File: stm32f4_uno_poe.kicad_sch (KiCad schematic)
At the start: 13 parts, among them J101 STM32 GPIO, J102 Digital/PWM, J103 STM32 GPIO, J104 STM32 GPIO, J105 STM32 GPIO, J106 Power, J107 Conn_01x04, J108 Ethernet, J109 STM32 GPIO, J110 Digital/PWM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

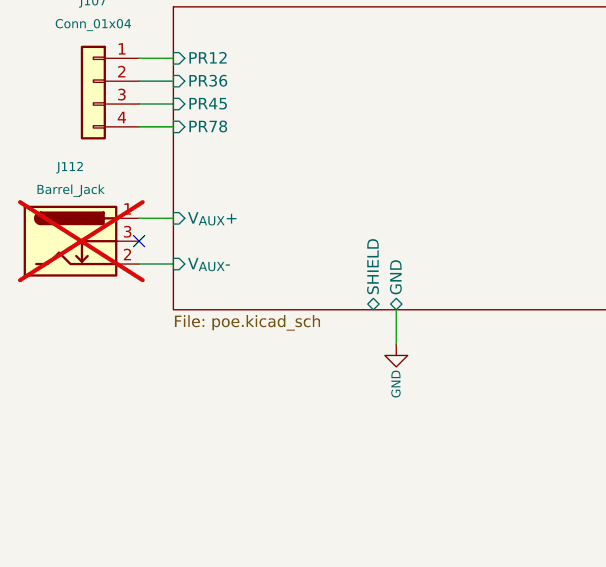
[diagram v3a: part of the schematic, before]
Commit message: Set DNP
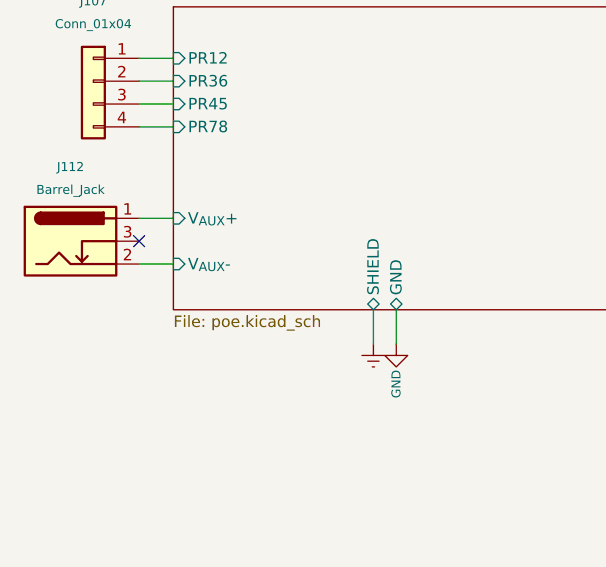
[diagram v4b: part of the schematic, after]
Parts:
- J104, J106, J107, J108, J111, J113: now left out of the parts list
- J112: now fitted; now left out of the parts list
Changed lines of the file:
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@@
     (stroke (width 0) (type solid))
+  )
+  (wire (pts (xy 85.725 85.09) (xy 85.725 88.9))
+    (stroke (width 0) (type default))
   )
   (wire (pts (xy 267.335 29.845) (xy 280.035 29.845))
@@
   )
   (symbol (lib_id "Connector_Generic:Conn_01x08") (at 189.865 45.085 0) (unit 1)
-    (in_bom yes) (on_board yes) (dnp no)
+    (in_bom no) (on_board yes) (dnp no)
     (property "Reference" "J106" (at 189.865 34.925 0)
       (effects (font (size 1 1)))
@@
     (property "Datasheet" "" (at 189.865 45.085 0)
       (effects (font (size 1 1)))
+    )
+    (property "Description" "" (at 189.865 45.085 0)
+      (effects (font (size 1.27 1.27)) hide)
+    )
+    (property "Manufacturer" "" (at 189.865 45.085 0)
+      (effects (font (size 1.27 1.27)) hide)
+    )
+    (property "Partnumber" "" (at 189.865 45.085 0)
+      (effects (font (size 1.27 1.27)) hide)
+    )
+    (property "JLCPCB Part #" "" (at 189.865 45.085 0)
+      (effects (font (size 1.27 1.27)) hide)
+    )
+    (property "isBasicPart" "" (at 189.865 45.085 0)
+      (effects (font (size 1.27 1.27)) hide)
+    )
+    (property "Description" "" (at 189.865 45.085 0)
+      (effects (font (size 1.27 1.27)) hide)
+    )
+    (property "Manufacturer" "" (at 189.865 45.085 0)
+      (effects (font (size 1.27 1.27)) hide)
+    )
+    (property "Partnumber" "" (at 189.865 45.085 0)
+      (effects (font (size 1.27 1.27)) hide)
+    )
+    (property "JLCPCB Part #" "" (at 189.865 45.085 0)
+      (effects (font (size 1.27 1.27)) hide)
+    )
+    (property "isBasicPart" "" (at 189.865 45.085 0)
+      (effects (font (size 1.27 1.27)) hide)
     )
     (pin "1")
@@
   )
   (symbol (lib_id "Connector_Generic:Conn_01x06") (at 189.865 70.485 0) (unit 1)
-    (in_bom yes) (on_board yes) (dnp no)
+    (in_bom no) (on_board yes) (dnp no)
     (property "Reference" "J111" (at 189.865 62.865 0)
       (effects (font (size 1 1)))
@@
     (property "Datasheet" "~" (at 189.865 70.485 0)
       (effects (font (size 1 1)) hide)
+    )
+    (property "Description" "" (at 189.865 70.485 0)
+      (effects (font (size 1.27 1.27)) hide)
+    )
+    (property "Manufacturer" "" (at 189.865 70.485 0)
+      (effects (font (size 1.27 1.27)) hide)
+    )
+    (property "Partnumber" "" (at 189.865 70.485 0)
+      (effects (font (size 1.27 1.27)) hide)
+    )
+    (property "JLCPCB Part #" "" (at 189.865 70.485 0)
+      (effects (font (size 1.27 1.27)) hide)
+    )
+    (property "isBasicPart" "" (at 189.865 70.485 0)
+      (effects (font (size 1.27 1.27)) hide)
+    )
+    (property "Description" "" (at 189.865 70.485 0)
+      (effects (font (size 1.27 1.27)) hide)
+    )
+    (property "Manufacturer" "" (at 189.865 70.485 0)
+      (effects (font (size 1.27 1.27)) hide)
+    )
+    (property "Partnumber" "" (at 189.865 70.485 0)
+      (effects (font (size 1.27 1.27)) hide)
+    )
+    (property "JLCPCB Part #" "" (at 189.865 70.485 0)
+      (effects (font (size 1.27 1.27)) hide)
+    )
+    (property "isBasicPart" "" (at 189.865 70.485 0)
+      (effects (font (size 1.27 1.27)) hide)
     )
     (pin "1")
@@
   )
   (symbol (lib_id "Connector:Barrel_Jack_Switch") (at 52.07 77.47 0) (unit 1)
-    (in_bom yes) (on_board yes) (dnp yes) (fields_autoplaced)
+    (in_bom no) (on_board yes) (dnp no) (fields_autoplaced)
     (property "Reference" "J112" (at 52.07 69.215 0)
       (effects (font (size 1 1)))
@@
   )
   (symbol (lib_id "Connector_Generic:Conn_01x10") (at 242.57 65.405 0) (mirror y) (unit 1)
-    (in_bom yes) (on_board yes) (dnp no)
+    (in_bom no) (on_board yes) (dnp no)
     (property "Reference" "J108" (at 242.57 52.705 0)
       (effects (font (size 1 1)))
@@
   )
   (symbol (lib_id "Connector_Generic:Conn_01x04") (at 54.61 59.69 0) (mirror y) (unit 1)
-    (in_bom yes) (on_board yes) (dnp no) (fields_autoplaced)
+    (in_bom no) (on_board yes) (dnp no) (fields_autoplaced)
     (property "Reference" "J107" (at 54.61 50.8 0)
       (effects (font (size 1 1)))
@@
   )
   (symbol (lib_id "Connector_Generic:Conn_01x08") (at 242.57 39.37 0) (mirror y) (unit 1)
-    (in_bom yes) (on_board yes) (dnp no)
+    (in_bom no) (on_board yes) (dnp no)
     (property "Reference" "J104" (at 242.57 29.21 0)
       (effects (font (size 1 1)))
@@
     (property "Datasheet" "" (at 242.57 39.37 0)
       (effects (font (size 1 1)))
+    )
+    (property "Description" "" (at 242.57 39.37 0)
+      (effects (font (size 1.27 1.27)) hide)
+    )
+    (property "Manufacturer" "" (at 242.57 39.37 0)
+      (effects (font (size 1.27 1.27)) hide)
+    )
+    (property "Partnumber" "" (at 242.57 39.37 0)
+      (effects (font (size 1.27 1.27)) hide)
+    )
+    (property "JLCPCB Part #" "" (at 242.57 39.37 0)
+      (effects (font (size 1.27 1.27)) hide)
+    )
+    (property "isBasicPart" "" (at 242.57 39.37 0)
+      (effects (font (size 1.27 1.27)) hide)
+    )
+    (property "Description" "" (at 242.57 39.37 0)
+      (effects (font (size 1.27 1.27)) hide)
+    )
+    (property "Manufacturer" "" (at 242.57 39.37 0)
+      (effects (font (size 1.27 1.27)) hide)
+    )
+    (property "Partnumber" "" (at 242.57 39.37 0)
+      (effects (font (size 1.27 1.27)) hide)
+    )
+    (property "JLCPCB Part #" "" (at 242.57 39.37 0)
+      (effects (font (size 1.27 1.27)) hide)
+    )
+    (property "isBasicPart" "" (at 242.57 39.37 0)
+      (effects (font (size 1.27 1.27)) hide)
     )
     (pin "1")
@@
   )
   (symbol (lib_id "Connector_Generic:Conn_01x02") (at 128.27 57.15 0) (unit 1)
-    (in_bom yes) (on_board yes) (dnp no) (fields_autoplaced)
+    (in_bom no) (on_board yes) (dnp no) (fields_autoplaced)
     (property "Reference" "J113" (at 130.81 57.15 0)
       (effects (font (size 1.27 1.27)) (justify left))
@@
     )
     (property "Datasheet" "~" (at 128.27 57.15 0)
+      (effects (font (size 1.27 1.27)) hide)
+    )
+    (property "Description" "" (at 128.27 57.15 0)
+      (effects (font (size 1.27 1.27)) hide)
+    )
+    (property "Manufacturer" "" (at 128.27 57.15 0)
+      (effects (font (size 1.27 1.27)) hide)
+    )
+    (property "Partnumber" "" (at 128.27 57.15 0)
+      (effects (font (size 1.27 1.27)) hide)
+    )
+    (property "JLCPCB Part #" "" (at 128.27 57.15 0)
+      (effects (font (size 1.27 1.27)) hide)
+    )
+    (property "isBasicPart" "" (at 128.27 57.15 0)
+      (effects (font (size 1.27 1.27)) hide)
+    )
+    (property "Description" "" (at 128.27 57.15 0)
+      (effects (font (size 1.27 1.27)) hide)
+    )
+    (property "Manufacturer" "" (at 128.27 57.15 0)
+      (effects (font (size 1.27 1.27)) hide)
+    )
+    (property "Partnumber" "" (at 128.27 57.15 0)
+      (effects (font (size 1.27 1.27)) hide)
+    )
+    (property "JLCPCB Part #" "" (at 128.27 57.15 0)
+      (effects (font (size 1.27 1.27)) hide)
+    )
+    (property "isBasicPart" "" (at 128.27 57.15 0)
       (effects (font (size 1.27 1.27)) hide)
     )
@@
         )
       )
+    )
+  )
+  (symbol (lib_id "power:Earth") (at 85.725 88.9 0) (unit 1)
+    (in_bom yes) (on_board yes) (dnp no) (fields_autoplaced)
+    (property "Reference" "#PWR0109" (at 85.725 95.25 0)
+      (effects (font (size 1.27 1.27)) hide)
+    )
+    (property "Value" "Earth" (at 85.725 92.71 0)
+      (effects (font (size 1.27 1.27)) hide)
+    )
+    (property "Footprint" "" (at 85.725 88.9 0)
+      (effects (font (size 1.27 1.27)) hide)
+    )
+    (property "Datasheet" "~" (at 85.725 88.9 0)
+      (effects (font (size 1.27 1.27)) hide)
+    )
+    (pin "1")
+    (instances
+      (project "stm32f4_uno_poe"
+        (path "/e63e39d7-6ac0-4ffd-8aa3-1841a4541b55"
+          (reference "#PWR0109") (unit 1)
+        )
+      )

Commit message: #1 Use new central library KiCad-Lib
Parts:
- J113: footprint (none) -> Connector_PinHeader_2.54mm:PinHeader_1x02_P2.54mm_Vertical
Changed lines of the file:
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@@
       (effects (font (size 1.27 1.27)) (justify left))
     )
-    (property "Footprint" "" (at 128.27 57.15 0)
+    (property "Footprint" "Connector_PinHeader_2.54mm:PinHeader_1x02_P2.54mm_Vertical" (at 128.27 57.15 0)
       (effects (font (size 1.27 1.27)) hide)
     )

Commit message: #1 Use new central library KiCad-Lib
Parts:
- J112: footprint Connector_BarrelJack:BarrelJack_CUI_PJ-102AH_Horizontal -> #Connector:CUI Devices PJ-102AH.pdf; symbol Connector:Barrel_Jack_Switch -> #Connector:CUI Devices PJ-102AH
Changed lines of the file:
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@@
     )
   )
-  (symbol (lib_id "Connector:Barrel_Jack_Switch") (at 52.07 77.47 0) (unit 1)
+  (symbol (lib_id "#Connector:CUI Devices PJ-102AH") (at 52.07 77.47 0) (unit 1)
     (in_bom no) (on_board yes) (dnp no) (fields_autoplaced)
     (property "Reference" "J112" (at 52.07 69.215 0)
@@
       (effects (font (size 1 1)))
     )
-    (property "Footprint" "Connector_BarrelJack:BarrelJack_CUI_PJ-102AH_Horizontal" (at 53.34 78.486 0)
-      (effects (font (size 1 1)) hide)
+    (property "Footprint" "#Connector:CUI Devices PJ-102AH.pdf" (at 53.34 78.486 0)
+      (effects (font (size 1.27 1.27)) hide)
     )
-    (property "Datasheet" "~" (at 53.34 78.486 0)
-      (effects (font (size 1 1)) hide)
+    (property "Datasheet" "${KIPRJMOD}/KiCad-Lib/#Connector.doc/CUI Devices PJ-102AH.pdf" (at 53.34 78.486 0)
+      (effects (font (size 1.27 1.27)) hide)
     )
     (property "Description" "" (at 52.07 77.47 0)

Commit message: WIP
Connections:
- net V_{IN} is gone; now on net PoE/+24V: J106.8 (Pin_8)
- net PoE/24V renamed PoE/+24V
- no-connect marks 75 -> 74
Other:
- sheet PoE ports: added +24V; removed 24V
- note added: "V_{IN}"
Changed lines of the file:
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@@
   (junction (at 176.53 45.085) (diameter 0) (color 0 0 0 0)
+  )
+  (junction (at 121.92 57.15) (diameter 0) (color 0 0 0 0)
   )
   (junction (at 176.53 51.435) (diameter 0) (color 0 0 0 0)
@@
   (no_connect (at 267.335 37.465))
   (no_connect (at 247.65 46.99))
-  (no_connect (at 184.785 55.245))
   (no_connect (at 199.39 42.545))
   (no_connect (at 184.785 37.465))
@@
     (stroke (width 0) (type solid))
   )
-  (wire (pts (xy 119.38 57.15) (xy 123.19 57.15))
+  (wire (pts (xy 119.38 57.15) (xy 121.92 57.15))
     (stroke (width 0) (type default))
   )
@@
     (stroke (width 0) (type default))
   )
-  (wire (pts (xy 176.53 55.245) (xy 184.785 55.245))
+  (wire (pts (xy 121.92 55.245) (xy 184.785 55.245))
     (stroke (width 0) (type default))
   )
@@
     (stroke (width 0) (type default))
   )
+  (wire (pts (xy 121.92 57.15) (xy 123.19 57.15))
+    (stroke (width 0) (type default))
+  )
   (wire (pts (xy 267.335 42.545) (xy 280.035 42.545))
     (stroke (width 0) (type solid))
@@
     (stroke (width 0) (type default))
   )
+  (wire (pts (xy 121.92 57.15) (xy 121.92 55.245))
+    (stroke (width 0) (type default))
+  )
   (wire (pts (xy 267.335 29.845) (xy 280.035 29.845))
     (stroke (width 0) (type solid))
@@
   (text "D7" (at 280.035 60.325 0)
     (effects (font (size 1 1)) (justify right bottom))
+  )
+  (text "V_{IN}" (at 176.53 55.245 0)
+    (effects (font (size 1 1)) (justify left bottom))
   )
   (text "D10*" (at 280.035 45.085 0)
@@
   (label "PB9" (at 267.335 29.845 0) (fields_autoplaced)
     (effects (font (size 1 1)) (justify left bottom))
-  )
-  (label "V_{IN}" (at 184.785 55.245 180) (fields_autoplaced)
-    (effects (font (size 1 1)) (justify right bottom))
   )
   (label "PE2" (at 199.39 62.865 180) (fields_autoplaced)
@@
       (effects (font (size 1.27 1.27)) (justify left))
     )
-    (pin "24V" output (at 119.38 57.15 0)
+    (pin "+24V" output (at 119.38 57.15 0)
       (effects (font (size 1.27 1.27)) (justify right))
     )
